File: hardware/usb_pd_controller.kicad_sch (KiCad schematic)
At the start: 28 parts, among them Q1 BSS138, Q2 BSS138, Q3 IRF7855TRPBF, Q4 IRF7855TRPBF, U1 AP33772SDKZ-13-FA02

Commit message: usb_pd_controller: C3 1uF -> 2.2uF/50V X7R (REV_C 3.1 #3)
cSnkBulk minimumu olan 1 uF'ı DC bias altında garanti etmek için.
Footprint 0805'te bırakıldı; doküman footprint belirtmiyor. 50 V bias
altında 0805 X7R'nin efektif kapasitesi 1 uF hedefinin altına düşebilir,
1206'ya çıkarmak değerlendirilmeli.

Co-Authored-By: Claude Opus 5 <noreply@anthropic.com>
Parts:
- C3: value 1uF / 50V -> 2.2uF / 50V X7R
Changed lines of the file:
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@@
 			)
 		)
-		(property "Value" "1uF / 50V"
+		(property "Value" "2.2uF / 50V X7R"
 			(at 86.36 35.56 0)
 			(show_name no)

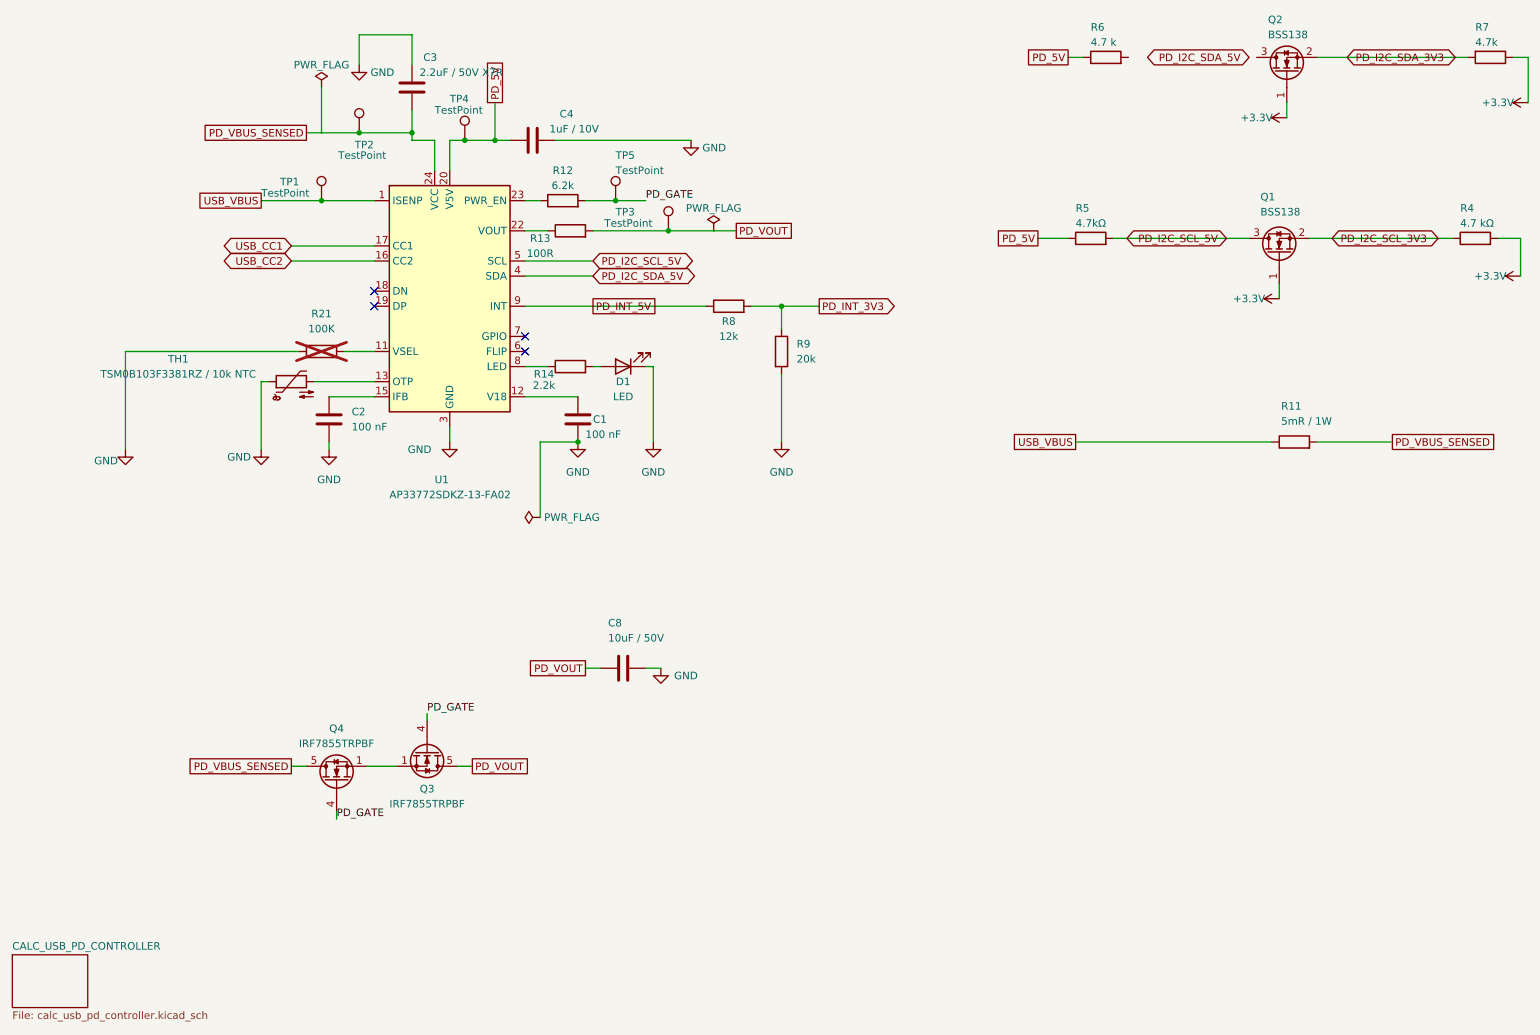
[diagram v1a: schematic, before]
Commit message: usb_pd_controller, mcu, powersensing: çizimleri yeniden düzenle, SDA dönüştürücüsünü bağla
Çizim (netlist aşağıdaki düzeltme dışında aynı)
- usb_pd_controller: üç blok (AP33772S kontrolcü, VBUS şönt + çıkış
  anahtarı, I2C seviye dönüştürücü). Q3/Q4 kapıları tek tel hattıyla,
  Q3 ang 90 + mirror y. TestPoint değer yazıları gizli.
- mcu: ESP32, RTC ve test noktası blokları. Sağ kenar satırları kesişmesiz;
  GPIO8 strap ağı satır sonunda, GPIO9 BOOT ağı dıştan aşağı. EN RC + RESET
  IC'nin üstüne alındı. UART/I2C/INT test noktaları etiketle ayrı blokta.
- powersensing: INA228 bloğu, şönt Kelvin bağlantısı kesişmesiz.

Devre düzeltmesi (kullanıcı onaylı)
- SDA seviye dönüştürücüsü kopuktu: R6.2 ve Q2.D bağlı değildi,
  PD_I2C_SDA_5V etiketi boştaydı. SCL tarafıyla (R5/Q1) simetrik bağlandı.
- Netlist farkı: PD_I2C_SDA_5V += Q2.3, R6.2;
  unconnected-(Q2-D-Pad3) ve unconnected-(R6-Pad2) kalktı.
- ERC 5 -> 2 (0 hata). Kalanlar: TL431DBZ lib_symbol_mismatch, OUT_EN
  isolated_pin_label (GPIO seçimi bekliyor).

Co-Authored-By: Claude Opus 5 <noreply@anthropic.com>
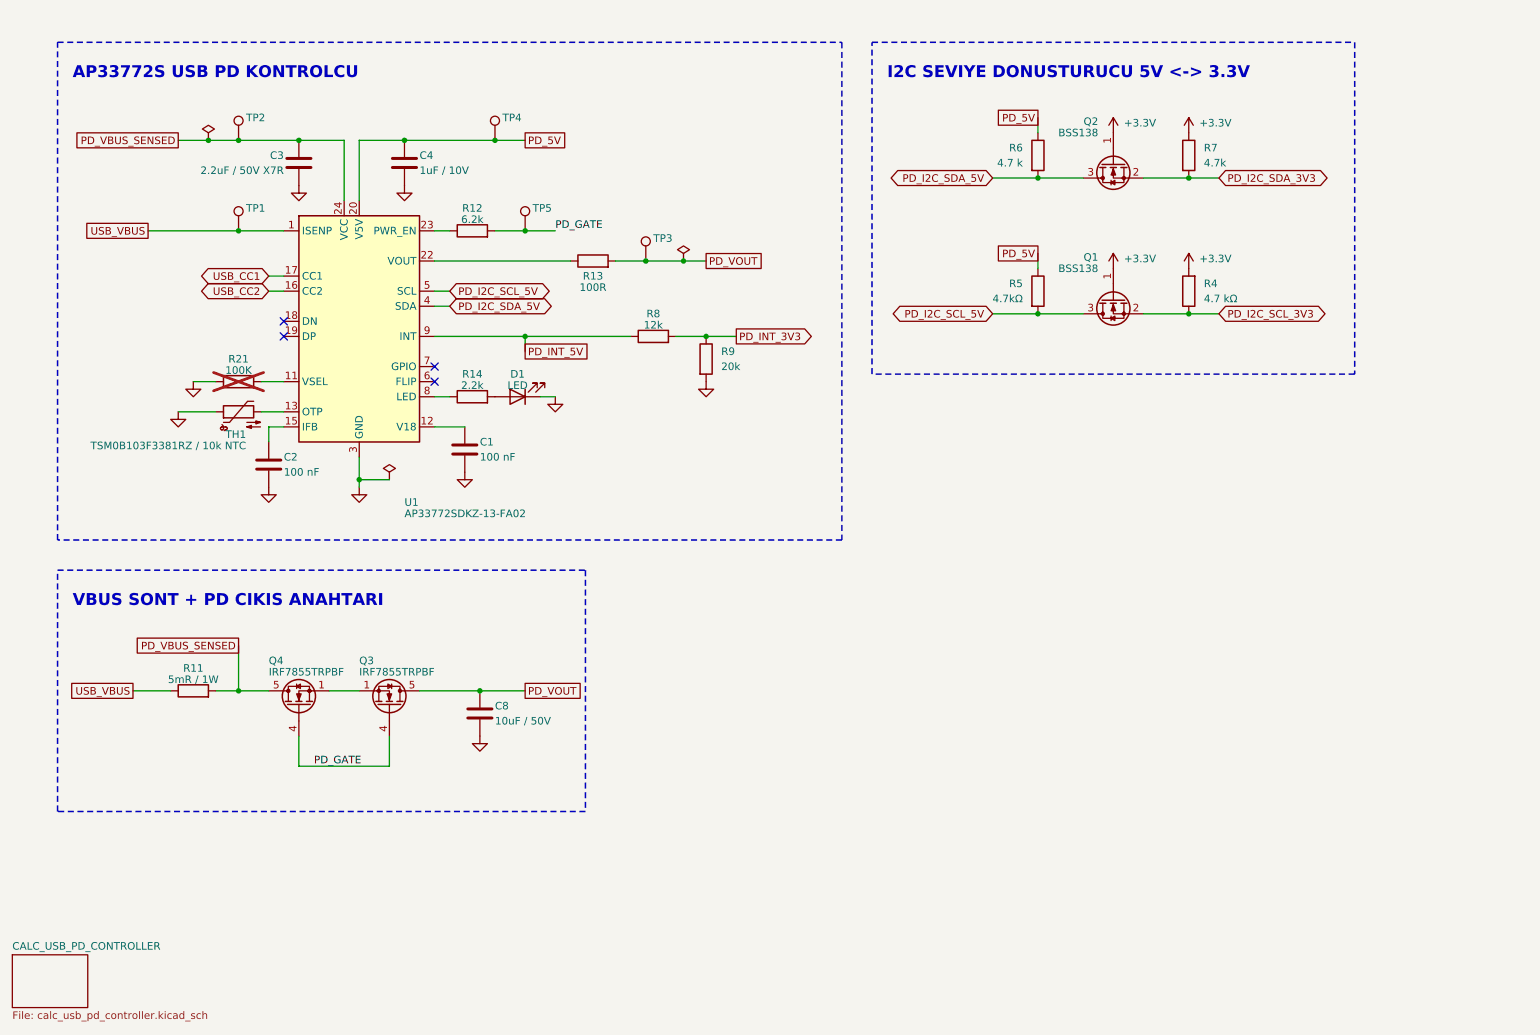
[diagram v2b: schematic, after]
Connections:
- net PD_I2C_SDA_5V: now also Q2.3 (D), R6.2
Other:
- note added: "AP33772S USB PD KONTROLCU"
- note added: "I2C SEVIYE DONUSTURUCU 5V <-> 3.3V"
- note added: "VBUS SONT + PD CIKIS ANAHTARI"
- moved on the sheet: C1, C2, C3, C4, C8, D1, Q1, Q2, Q3, Q4, R11, R12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
